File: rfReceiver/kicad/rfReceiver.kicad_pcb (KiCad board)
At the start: 2 copper layers, 13 parts, among them J1 MAX485AB, J2 RF module, J3 POWER, Q1 BC547, U1 MAX485E

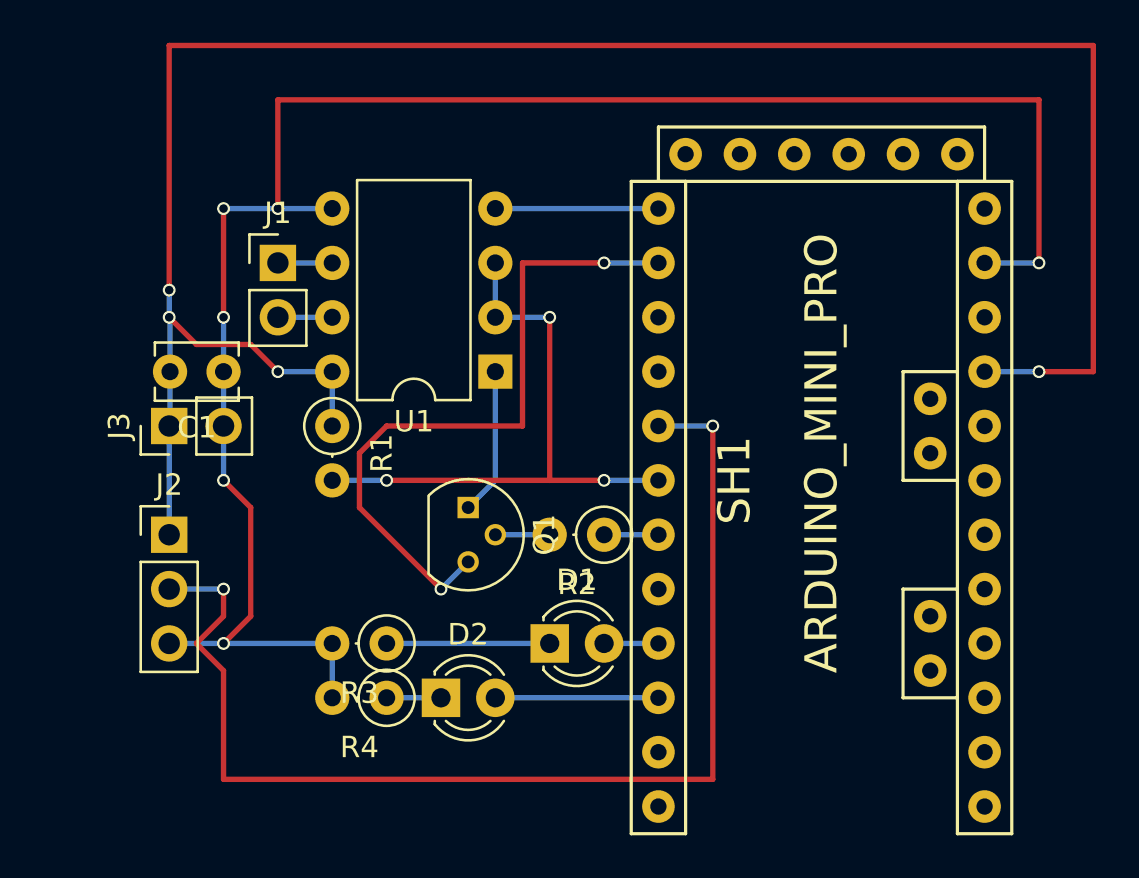
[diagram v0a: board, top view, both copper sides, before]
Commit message: update kicad schema
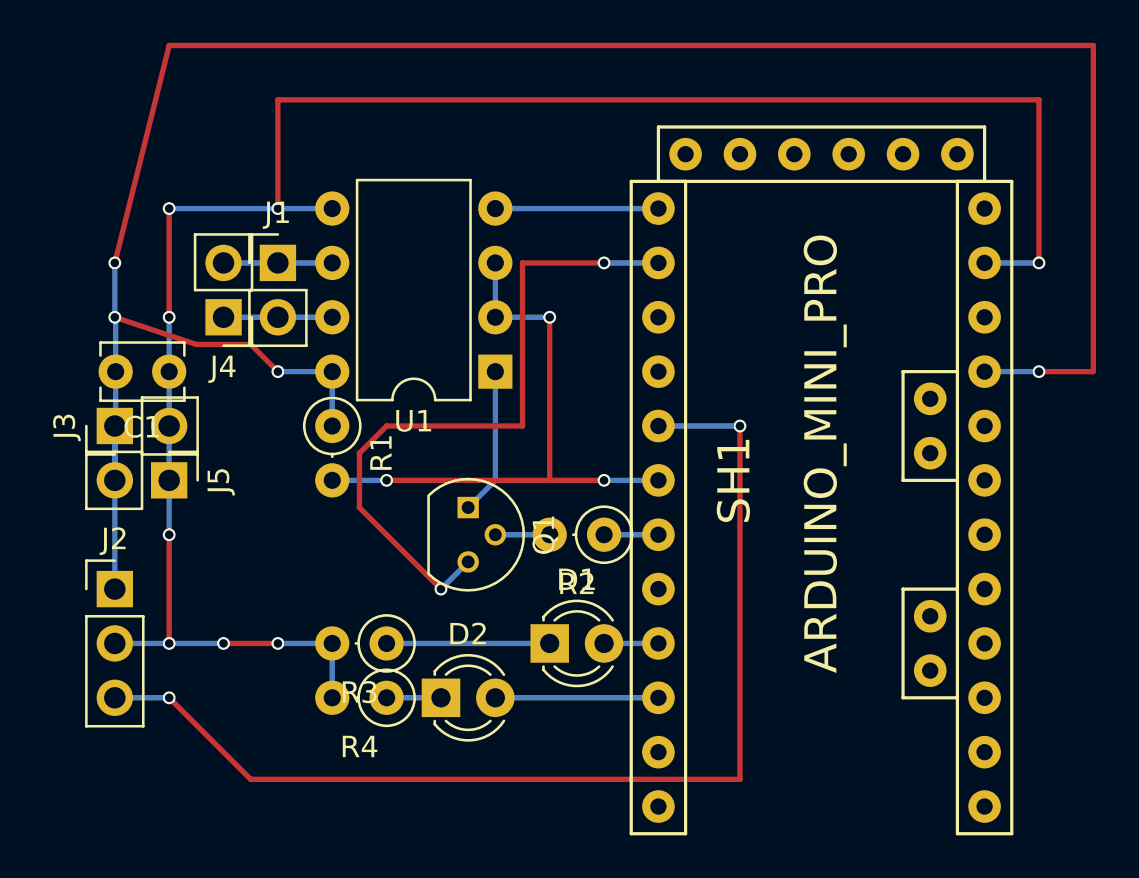
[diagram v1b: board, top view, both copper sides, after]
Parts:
- added J4: MAX485AB_FW, Socket_Strips:Socket_Strip_Straight_1x02_Pitch2.54mm, F.Cu at (147.3, 76.2)
- added J5: POWER_FW, Socket_Strips:Socket_Strip_Straight_1x02_Pitch2.54mm, F.Cu at (144.8, 83.8)
- moved J2 3.59 mm to (142.2, 88.9)
- moved C1 2.54 mm to (144.8, 78.7)
- moved J3 2.54 mm to (142.2, 81.3)
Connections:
- net Net-(J1-Pad1) renamed /MAX485A
- net Net-(J1-Pad2) renamed /MAX485B
- J2 pad 2: /RFData -> GND
- J2 pad 3: GND -> /RFData
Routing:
- net +5V: track 97.7 -> 105.3 mm
- net GND: track 87.4 -> 91.4 mm, vias 6 -> 8
- net /RFData: track 54.4 -> 51.1 mm
- net /MAX485B: track 2.54 -> 5.08 mm
- net /MAX485A: track 2.54 -> 5.08 mm
